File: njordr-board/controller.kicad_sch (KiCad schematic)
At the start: 21 parts, among them Q1 MMBT2222A, SW1 RST, SW2 BOOT, U4 ESP32-S3, U5 GD25QxxxEY, Y1 40 MHz, Y2 32.768 kHz

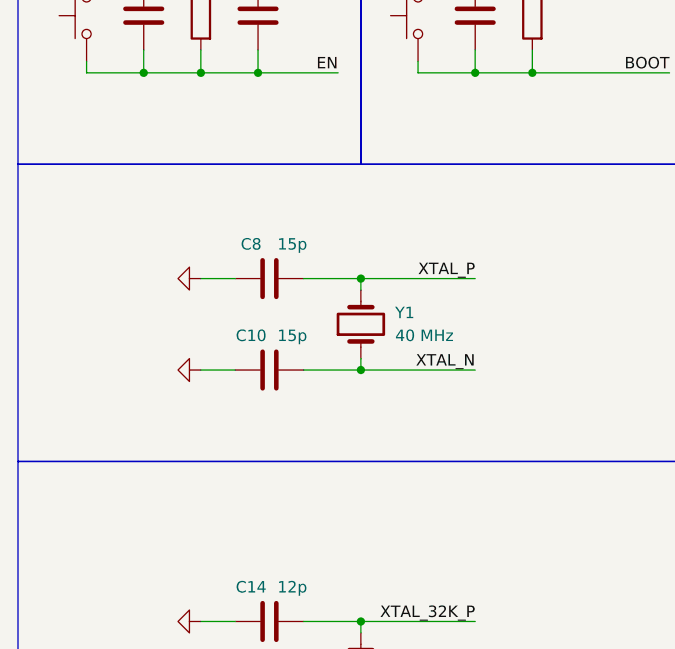
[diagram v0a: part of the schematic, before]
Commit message: njordr-board: Use updated library symbols and packages
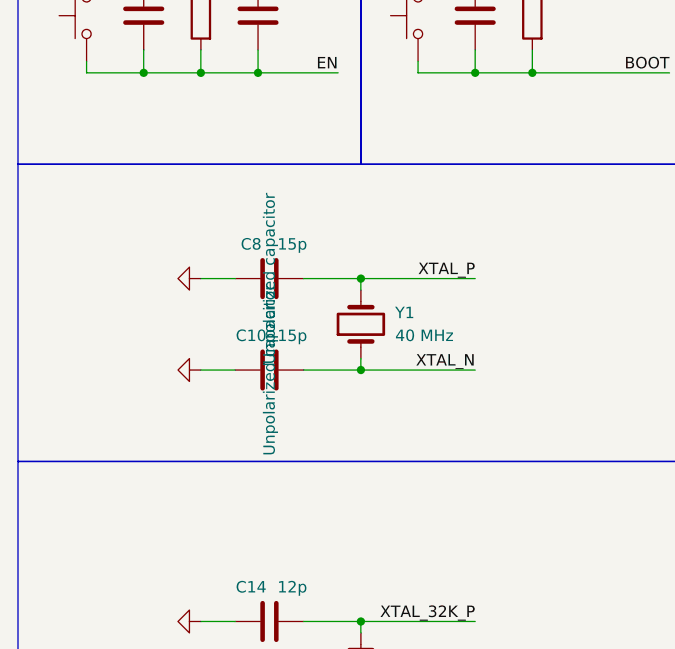
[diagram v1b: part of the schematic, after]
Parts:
- C10, C14, C15, C16, C4, C5, C8: footprint Capacitor_SMD:C_0603_1608Metric_Pad1.08x0.95mm_HandSolder -> njordr:C-0603-HandSolder
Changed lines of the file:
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@@
 			)
 		)
-		(property "Description" ""
+		(property "Description" "Resistor"
 			(at 325.12 81.28 0)
 			(effects
@@
 			)
 		)
-		(property "Footprint" "Capacitor_SMD:C_0603_1608Metric_Pad1.08x0.95mm_HandSolder"
+		(property "Footprint" "njordr:C-0603-HandSolder"
 			(at 57.15 90.4748 0)
 			(effects
@@
 			)
 		)
-		(property "Datasheet" "https://jlcpcb.com/parts/componentSearch?searchTxt=15p%200603"
+		(property "Datasheet" "~"
 			(at 53.34 91.44 0)
 			(effects
@@
 			)
 		)
-		(property "Description" ""
+		(property "Description" "Unpolarized capacitor"
 			(at 53.34 91.44 0)
 			(effects
@@
 			)
 		)
-		(property "Footprint" "Capacitor_SMD:C_0603_1608Metric_Pad1.08x0.95mm_HandSolder"
+		(property "Footprint" "njordr:C-0603-HandSolder"
 			(at 75.2348 48.26 0)
 			(effects
@@
 			)
 		)
-		(property "Description" ""
+		(property "Description" "Unpolarized capacitor"
 			(at 76.2 52.07 0)
 			(effects
@@
 			)
 		)
-		(property "Datasheet" "https://jlcpcb.com/partdetail/26547-0603WAF1002T5E/C25804"
+		(property "Datasheet" "~"
 			(at 45.72 52.07 0)
 			(effects
@@
 	)
 	(symbol
-		(lib_name "GND_1")
 		(lib_id "power:GND")
 		(at 45.72 119.38 270)
@@
 	)
 	(symbol
-		(lib_name "GND_1")
 		(lib_id "power:GND")
 		(at 39.37 43.18 0)
@@
 			)
 		)
-		(property "Datasheet" "https://jlcpcb.com/partdetail/SeikoEpson-Q13FC13500004/C32346"
+		(property "Datasheet" "~"
 			(at 63.5 124.46 0)
 			(effects
@@
 	)
 	(symbol
-		(lib_name "GND_1")
 		(lib_id "power:GND")
 		(at 162.56 116.84 0)
@@
 	)
 	(symbol
-		(lib_name "GND_1")
 		(lib_id "power:GND")
 		(at 52.07 43.18 0)
@@
 	)
 	(symbol
-		(lib_name "GND_1")
 		(lib_id "power:GND")
 		(at 334.01 101.6 0)
@@
 			)
 		)
-		(property "Footprint" "Capacitor_SMD:C_0603_1608Metric_Pad1.08x0.95mm_HandSolder"
+		(property "Footprint" "njordr:C-0603-HandSolder"
 			(at 57.15 128.5748 0)
 			(effects
@@
 			)
 		)
-		(property "Datasheet" "https://jlcpcb.com/partdetail/39506-CL10C120JB8NNNC/C38523"
+		(property "Datasheet" "~"
 			(at 53.34 129.54 0)
 			(effects
@@
 			)
 		)
-		(property "Description" ""
+		(property "Description" "Unpolarized capacitor"
 			(at 53.34 129.54 0)
 			(effects
@@
 			)
 		)
-		(property "Datasheet" "https://jlcpcb.com/partdetail/26547-0603WAF1002T5E/C25804"
+		(property "Datasheet" "~"
 			(at 54.61 165.1 0)
 			(effects
@@
 			)
 		)
-		(property "Datasheet" "https://jlcpcb.com/partdetail/TOGNJING-XOS25040000LT00351005/C37635410"
+		(property "Datasheet" "~"
 			(at 63.5 86.36 0)
 			(effects
@@
 	)
 	(symbol
-		(lib_name "GND_1")
 		(lib_id "power:GND")
 		(at 45.72 91.44 270)
@@
 	)
 	(symbol
-		(lib_name "GND_1")
 		(lib_id "power:GND")
 		(at 69.85 43.18 0)
@@
 			)
 		)
-		(property "Footprint" "Capacitor_SMD:C_0603_1608Metric_Pad1.08x0.95mm_HandSolder"
+		(property "Footprint" "njordr:C-0603-HandSolder"
 			(at 38.4048 48.26 0)
 			(effects
@@
 			)
 		)
-		(property "Description" ""
+		(property "Description" "Unpolarized capacitor"
 			(at 39.37 52.07 0)
 			(effects
@@
 	)
 	(symbol
-		(lib_name "GND_1")
 		(lib_id "power:GND")
 		(at 45.72 129.54 270)
@@
 			)
 		)
-		(property "Footprint" "Capacitor_SMD:C_0603_1608Metric_Pad1.08x0.95mm_HandSolder"
+		(property "Footprint" "njordr:C-0603-HandSolder"
 			(at 57.15 118.4148 0)
 			(effects
@@
 			)
 		)
-		(property "Datasheet" "https://jlcpcb.com/partdetail/39506-CL10C120JB8NNNC/C38523"
+		(property "Datasheet" "~"
 			(at 53.34 119.38 0)
 			(effects
@@
 			)
 		)
-		(property "Description" ""
+		(property "Description" "Unpolarized capacitor"
 			(at 53.34 119.38 0)
 			(effects
@@
 			)
 		)
-		(property "Datasheet" "https://jlcpcb.com/partdetail/26547-0603WAF1002T5E/C25804"
+		(property "Datasheet" "~"
 			(at 82.55 52.07 0)
 			(effects
@@
 			)
 		)
-		(property "Footprint" "Capacitor_SMD:C_0603_1608Metric_Pad1.08x0.95mm_HandSolder"
+		(property "Footprint" "njordr:C-0603-HandSolder"
 			(at 57.15 80.3148 0)
 			(effects
@@
 			)
 		)
-		(property "Datasheet" "https://jlcpcb.com/parts/componentSearch?searchTxt=15p%200603"
+		(property "Datasheet" "~"
 			(at 53.34 81.28 0)
 			(effects
@@
 			)
 		)
-		(property "Description" ""
+		(property "Description" "Unpolarized capacitor"
 			(at 53.34 81.28 0)
 			(effects
@@
 	)
 	(symbol
-		(lib_name "GND_1")
 		(lib_id "power:GND")
 		(at 45.72 81.28 270)
@@
 			)
 		)
-		(property "Description" ""
+		(property "Description" "Resistor"
 			(at 334.01 81.28 0)
 			(effects
@@
 	)
 	(symbol
-		(lib_name "GND_1")
 		(lib_id "power:GND")
 		(at 76.2 43.18 0)
@@
 			)
 		)
-		(property "Footprint" "Capacitor_SMD:C_0603_1608Metric_Pad1.08x0.95mm_HandSolder"
+		(property "Footprint" "njordr:C-0603-HandSolder"
 			(at 51.1048 48.26 0)
 			(effects
@@
 			)
 		)
-		(property "Description" ""
+		(property "Description" "Unpolarized capacitor"
 			(at 52.07 52.07 0)
 			(effects
@@
 	)
 	(symbol
-		(lib_name "GND_1")
 		(lib_id "power:GND")
 		(at 33.02 43.18 0)
@@
 			)
 		)
-		(property "Datasheet" "https://jlcpcb.com/partdetail/26547-0603WAF1002T5E/C25804"
+		(property "Datasheet" "~"
 			(at 63.5 165.1 0)
 			(effects
